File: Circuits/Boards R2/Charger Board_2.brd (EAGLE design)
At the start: 63.5 x 50.8 mm, 80 parts, among them CON1 ISP(2X3), CON10 HEADER_3X1, CON11 HEADER_3X1, CON12 HEADER_3X1, CON13 HEADER_4X1, CON2 SCREWTERMINAL_1X2, CON3 HEADER_3X1, CON4 HEADER_3X1, CON5 HEADER_3X1, CON6 HEADER_3X1, CON7 HEADER_3X1, CON8 HEADER_3X1, CON9 HEADER_3X1, IC1 NCP1117DT33G, T1 NPN2N2222, T2 NPN2N2222, T3 SI4421DY, U1 ATMEGA324P, U2 ACS711, U3 JOYSTICKPTH, U4 MX25L25735E

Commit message: 
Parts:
- added CON14, CON15: HEADER_3X1, Mechanical:3PINHEADER_.100"
- B1: value PIEZOBUZZER -> PIEZOBUZZERPTH; device Passive:PIEZOBUZZER_HORIZONTAL -> Passive:PIEZOBUZZER
- moved B1 205.6 mm to (-176.5, -27.9)
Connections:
- net +3V3: now also B1.1; no longer B1.P$1
- net N$9: now also B1.2; no longer B1.P$2
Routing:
- net +3V3: track 104.7 -> 99.7 mm
- net N$9: track 11.4 -> 8.90 mm
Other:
- board size 63.5 x 50.8 mm -> 101.6 x 81.3 mm
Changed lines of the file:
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@@
 <board>
 <plain>
-<wire x1="0" y1="0" x2="63.5" y2="0" width="0" layer="20"/>
-<wire x1="63.5" y1="0" x2="63.5" y2="50.8" width="0" layer="20"/>
-<wire x1="63.5" y1="50.8" x2="0" y2="50.8" width="0" layer="20"/>
-<wire x1="0" y1="50.8" x2="0" y2="0" width="0" layer="20"/>
+<wire x1="0" y1="0" x2="101.6" y2="0" width="0" layer="20"/>
+<wire x1="101.6" y1="0" x2="101.6" y2="81.28" width="0" layer="20"/>
+<wire x1="101.6" y1="81.28" x2="0" y2="81.28" width="0" layer="20"/>
+<wire x1="0" y1="81.28" x2="0" y2="0" width="0" layer="20"/>
 </plain>
 <attributes>
@@
 <element name="R7" library="Passive" package="0603" value="10k" x="6.35" y="27.94" rot="R270"/>
 <element name="CON1" library="Mechanical" package="PINHEADER(2X3)" value="ISP(2X3)" x="11.43" y="29.21" rot="R270"/>
-<element name="B1" library="Passive" package="PIEZOBUZZER_HORIZONTAL" value="PIEZOBUZZER" x="16.256" y="43.434"/>
 <element name="R8" library="Passive" package="0603" value="1k" x="6.35" y="41.91" rot="R90"/>
 <element name="T1" library="Passive" package="SOT23" value="NPN2N2222" x="8.89" y="38.1" rot="R180"/>
@@
 <element name="R23" library="Passive" package="0603" value="10k" x="-146.05" y="-34.29"/>
 <element name="R24" library="Passive" package="0603" value="10k" x="-149.86" y="-34.29"/>
+<element name="CON14" library="Mechanical" package="3PINHEADER_.100&quot;" value="HEADER_3X1" x="-156.21" y="-31.75"/>
+<element name="CON15" library="Mechanical" package="3PINHEADER_.100&quot;" value="HEADER_3X1" x="-165.1" y="-31.75"/>
+<element name="B1" library="Passive" package="PIEZOBUZZER" value="PIEZOBUZZERPTH" x="-176.53" y="-27.94"/>
 </elements>
 <signals>
@@
 </signal>
 <signal name="N$9">
-<contactref element="B1" pad="P$2"/>
 <contactref element="R8" pad="1"/>
 <contactref element="T1" pad="3"/>
@@
 <wire x1="8.66" y1="39.1" x2="6.35" y2="41.16" width="0.254" layer="1"/>
 <wire x1="8.89" y1="39.1" x2="14.462" y2="39.1" width="0.254" layer="1"/>
-<wire x1="14.462" y1="39.1" x2="16.256" y2="40.894" width="0.254" layer="1"/>
+<contactref element="B1" pad="2"/>
+<wire x1="6.35" y1="41.16" x2="-173.99" y2="-27.94" width="0" layer="19" extent="1-1"/>
 </signal>
 <signal name="N$10">
@@
 <contactref element="C1" pad="1"/>
 <contactref element="R8" pad="2"/>
-<contactref element="B1" pad="P$1"/>
 <contactref element="R7" pad="1"/>
 <contactref element="IC1" pad="2"/>
@@
 <wire x1="6.35" y1="29.972" x2="6.35" y2="29.21" width="0.254" layer="16"/>
 <wire x1="6.35" y1="42.66" x2="12.692" y2="42.41" width="0.254" layer="1"/>
-<wire x1="12.692" y1="42.41" x2="16.256" y2="45.974" width="0.254" layer="1"/>
 <wire x1="6.35" y1="42.66" x2="5.58" y2="42.41" width="0.254" layer="1"/>
 <wire x1="5.58" y1="42.41" x2="5.08" y2="41.91" width="0.254" layer="1"/>
@@
 <contactref element="C15" pad="1"/>
 <contactref element="R23" pad="1"/>
+<contactref element="B1" pad="1"/>
+<wire x1="-146.8" y1="-34.29" x2="-179.07" y2="-27.94" width="0" layer="19" extent="1-1"/>
 <wire x1="-142.99" y1="-34.29" x2="-146.8" y2="-34.29" width="0" layer="19" extent="1-1"/>
 <wire x1="-135.255" y1="-35.255" x2="-142.99" y2="-34.29" width="0" layer="19" extent="1-1"/>

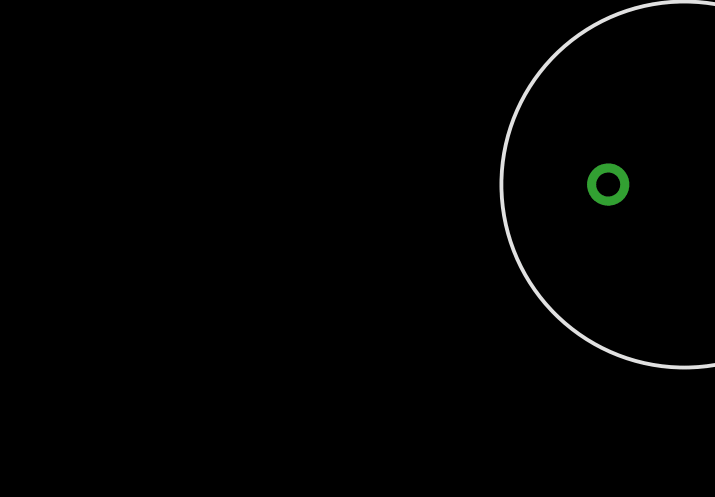
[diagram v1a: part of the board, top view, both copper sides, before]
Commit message: started adding rgb edge lighting hardware
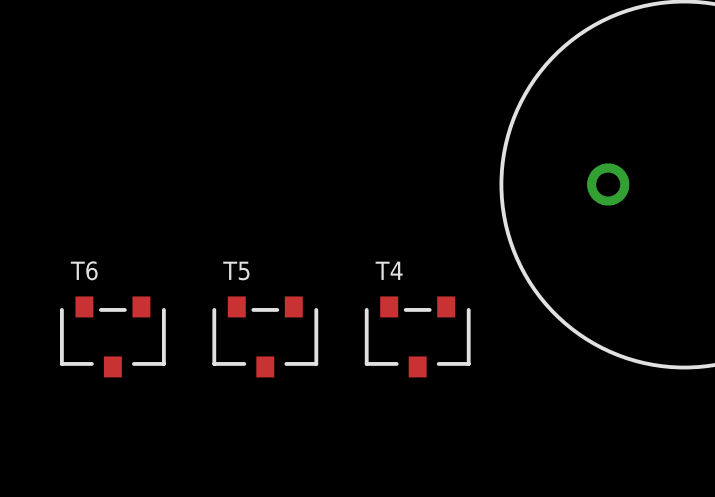
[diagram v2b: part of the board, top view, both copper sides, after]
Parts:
- added T4, T5, T6: NPN2N2222, Passive:SOT23
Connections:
- net GND: now also T4.2, T5.2, T6.2
- net LED1: now also T4.1
- net LED2: now also T5.1
- net LED3: now also T6.1
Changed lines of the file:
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@@
 <element name="CON15" library="Mechanical" package="3PINHEADER_.100&quot;" value="HEADER_3X1" x="-165.1" y="-31.75"/>
 <element name="B1" library="Passive" package="PIEZOBUZZER" value="PIEZOBUZZERPTH" x="-176.53" y="-27.94"/>
+<element name="T4" library="Passive" package="SOT23" value="NPN2N2222" x="-185.42" y="-33.02"/>
+<element name="T5" library="Passive" package="SOT23" value="NPN2N2222" x="-190.5" y="-33.02"/>
+<element name="T6" library="Passive" package="SOT23" value="NPN2N2222" x="-195.58" y="-33.02"/>
 </elements>
 <signals>
@@
 <contactref element="U4" pad="10"/>
 <contactref element="C15" pad="2"/>
+<contactref element="T4" pad="2"/>
+<contactref element="T5" pad="2"/>
+<contactref element="T6" pad="2"/>
+<wire x1="-191.45" y1="-32.02" x2="-196.53" y2="-32.02" width="0" layer="19" extent="1-1"/>
+<wire x1="-186.37" y1="-32.02" x2="-191.45" y2="-32.02" width="0" layer="19" extent="1-1"/>
+<wire x1="-141.49" y1="-34.29" x2="-186.37" y2="-32.02" width="0" layer="19" extent="1-1"/>
 <wire x1="-137.68" y1="-21.59" x2="-141.49" y2="-34.29" width="0" layer="19" extent="1-1"/>
 <wire x1="-134.0612" y1="-15.5194" x2="-137.68" y2="-21.59" width="0" layer="19" extent="1-1"/>
@@
 <wire x1="-18.05" y1="68.58" x2="-70.8" y2="61.96" width="0" layer="19" extent="1-1"/>
 <wire x1="9.84" y1="37.1" x2="-18.05" y2="68.58" width="0" layer="19" extent="1-1"/>
+<wire x1="12.7" y1="26.67" x2="11.43" y2="36.83" width="0" layer="19" extent="1-1"/>
+<wire x1="23.876" y1="29.21" x2="20.066" y2="25.4" width="0" layer="19" extent="1-1"/>
+<wire x1="28.321" y1="25.4" x2="24.13" y2="29.464" width="0" layer="19" extent="1-1"/>
+<wire x1="25.4" y1="21.59" x2="28.067" y2="25.146" width="0" layer="19" extent="1-1"/>
+<wire x1="39.37" y1="20.32" x2="32.25" y2="25.4" width="0" layer="19" extent="1-1"/>
+<wire x1="46.72" y1="25.4" x2="44.825" y2="20.955" width="0" layer="19" extent="1-1"/>
+<wire x1="3.81" y1="22.11" x2="12.7" y2="26.67" width="0" layer="19" extent="1-1"/>
+<wire x1="3.81" y1="15.24" x2="3.31" y2="20.82" width="0" layer="19" extent="1-1"/>
+<wire x1="3.81" y1="10.16" x2="3.81" y2="15.24" width="0" layer="19" extent="1-1"/>
+<wire x1="51.054" y1="12.954" x2="44.825" y2="20.955" width="0" layer="19" extent="1-1"/>
+<wire x1="13.97" y1="5.08" x2="3.81" y2="10.16" width="0" layer="19" extent="1-1"/>
+<wire x1="16.51" y1="5.08" x2="13.97" y2="5.08" width="0" layer="19" extent="1-1"/>
+<wire x1="19.05" y1="5.08" x2="16.51" y2="5.08" width="0" layer="19" extent="1-1"/>
+<wire x1="21.59" y1="5.08" x2="19.05" y2="5.08" width="0" layer="19" extent="1-1"/>
+<wire x1="24.13" y1="5.08" x2="21.59" y2="5.08" width="0" layer="19" extent="1-1"/>
+<wire x1="26.67" y1="5.08" x2="24.13" y2="5.08" width="0" layer="19" extent="1-1"/>
+<wire x1="29.21" y1="5.08" x2="26.67" y2="5.08" width="0" layer="19" extent="1-1"/>
+<wire x1="31.75" y1="5.08" x2="29.21" y2="5.08" width="0" layer="19" extent="1-1"/>
+<wire x1="34.29" y1="5.08" x2="31.75" y2="5.08" width="0" layer="19" extent="1-1"/>
+<wire x1="36.83" y1="5.08" x2="34.29" y2="5.08" width="0" layer="19" extent="1-1"/>
+<wire x1="58.42" y1="40.6" x2="53.705" y2="29.48" width="0" layer="19" extent="1-1"/>
 </signal>
 <signal name="RESET">
@@
 <wire x1="22.53" y1="31.15" x2="22.53" y2="33.85" width="0.254" layer="1"/>
 <contactref element="R21" pad="1"/>
+<contactref element="T4" pad="1"/>
+<wire x1="-66.79" y1="-8.89" x2="-184.47" y2="-32.02" width="0" layer="19" extent="1-1"/>
 <wire x1="22.53" y1="31.15" x2="-66.79" y2="-8.89" width="0" layer="19" extent="1-1"/>
 </signal>
@@
 <wire x1="21.73" y1="31.15" x2="21.73" y2="32.745" width="0.254" layer="1"/>
 <contactref element="R22" pad="1"/>
+<contactref element="T5" pad="1"/>
+<wire x1="-70.6" y1="-12.7" x2="-189.55" y2="-32.02" width="0" layer="19" extent="1-1"/>
 <wire x1="21.73" y1="31.15" x2="-70.6" y2="-12.7" width="0" layer="19" extent="1-1"/>
 </signal>
@@
 <contactref element="R1" pad="1"/>
 <contactref element="U1" pad="43"/>
+<contactref element="T6" pad="1"/>
+<wire x1="-70.6" y1="-8.89" x2="-194.63" y2="-32.02" width="0" layer="19" extent="1-1"/>
 <wire x1="20.93" y1="31.15" x2="-70.6" y2="-8.89" width="0" layer="19" extent="1-1"/>
 </signal>

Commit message: 
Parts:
- added C16, C19: 10uf, Passive:0805
- added C17, C18, C20, C21: .1uf, Passive:0603
- added CON16: HEADER_4X1, Mechanical:4PINHEADER_.100"
- added H5, H6, H7: MOUNTINGHOLE, Mechanical:MOUNTINGHOLE
- added LED7: IR, Passive:5MM_LED_RA
- added R25: 18, Passive:0603
- added R26, R29, R30: 1k, Passive:0603
- added T7, T8, T9: NPN2N2222, Passive:SOT23
- CON17, CON18: value FTDI_3PIN -> HEADER_3X1
- moved CON15 252.0 mm to (80.3, 25.4), turned to 90 degrees
- moved T6 248.5 mm to (46.0, 25.3), turned to 90 degrees
- moved T5 244.6 mm to (46.0, 29.5), turned to 90 degrees
- moved T4 240.8 mm to (46.0, 33.7), turned to 90 degrees
- moved CON14 231.6 mm to (63.0, 43.0), turned to 180 degrees
- moved B1 212.9 mm to (18.0, 58.5), turned to 270 degrees
- moved R24 212.9 mm to (59.4, 4.70)
- moved C12 207.1 mm to (85.7, 27.0), turned to 90 degrees
- moved C9 201.5 mm to (83.8, 27.0), turned to 90 degrees
- moved C8 200.1 mm to (84.8, 33.7), turned to 180 degrees
- moved C13 186.5 mm to (52.9, 39.9), turned to 270 degrees
- moved R15 184.8 mm to (54.9, 39.9), turned to 90 degrees
- moved R23 179.0 mm to (16.6, 40.3), turned to 90 degrees
- moved C15 174.8 mm to (17.3, 37.1)
- moved C7 171.7 mm to (89.5, 27.0), turned to 90 degrees
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- renumbered U$1 to CON17, U$2 to CON18
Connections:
- new net BLUE: CON16.1, T7.3
- new net GREEN: CON16.2, T8.3
- new net N$18: R26.1, T4.3, T7.1
- new net N$2: CON15.1, R16.1
- new net N$20: R29.1, T5.3, T8.1
- new net N$21: R30.1, T6.3, T9.1
- new net N$3: C12.1, C2.1, C6.1, C7.1, C8.1, C9.1, CON15.2, LED2.1, LED3.1, LED4.1, LED5.1, LED6.1, LED7.1
- new net N$5: C12.2, C2.2, C6.2, C7.2, C8.2, C9.2, CON15.3, T2.2
- new net N$6: LED7.2, R25.2
- new net RED: CON16.3, T9.3
- net +3V3: now also C16.1, C17.1, C18.1, C19.1, C20.1, C21.1, CON14.2
- net +5V: now also CON16.4, R26.2, R29.2, R30.2; no longer C12.1, C2.1, C6.1, C7.1, C8.1, C9.1, LED2.1, LED3.1, LED4.1, LED5.1, LED6.1
- net GND: now also C16.2, C17.2, C18.2, C19.2, C20.2, C21.2, CON14.3, CON17.1, CON18.1, T7.2, T8.2, T9.2; no longer C12.2, C2.2, C6.2, C7.2, C8.2, C9.2, CON17.3, CON18.3, T2.2
- net N$10: now also R25.1
- net N$19: now also CON18.3; no longer CON18.1
- net N$7: now also CON17.3; no longer CON17.1
- net TRANSMITLEDS: now also CON14.1; no longer R16.1
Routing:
- net +3V3: track 99.7 -> 229.9 mm, vias 4 -> 5
- net +5V: track 33.8 -> 121.2 mm
- net N$10: track 0.00 -> 68.4 mm
- net RESET: track 11.1 -> 54.3 mm
- net HORIZONTAL: track 0.00 -> 41.9 mm, vias 0 -> 2
- net TRANSMITLEDS: track 0.00 -> 41.3 mm
- net GND: track 39.6 -> 80.3 mm, vias 9 -> 15
- net VERTICAL: track 0.00 -> 37.9 mm
- net BUTTON: track 0.00 -> 36.4 mm
- net WP: track 0.00 -> 32.7 mm, vias 0 -> 2
- net LED3: track 0.00 -> 32.0 mm, vias 0 -> 2
- net LED2: track 1.59 -> 30.2 mm, vias 0 -> 2
- net CS: track 0.00 -> 26.7 mm, vias 0 -> 2
- net LED1: track 2.70 -> 28.8 mm, vias 0 -> 4
- net MISO: track 0.00 -> 25.0 mm
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- added copper zone on layer 1, net N$3
- added copper zone on layer 16, net N$5
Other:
- board size 101.6 x 81.3 mm -> 101.6 x 69.8 mm

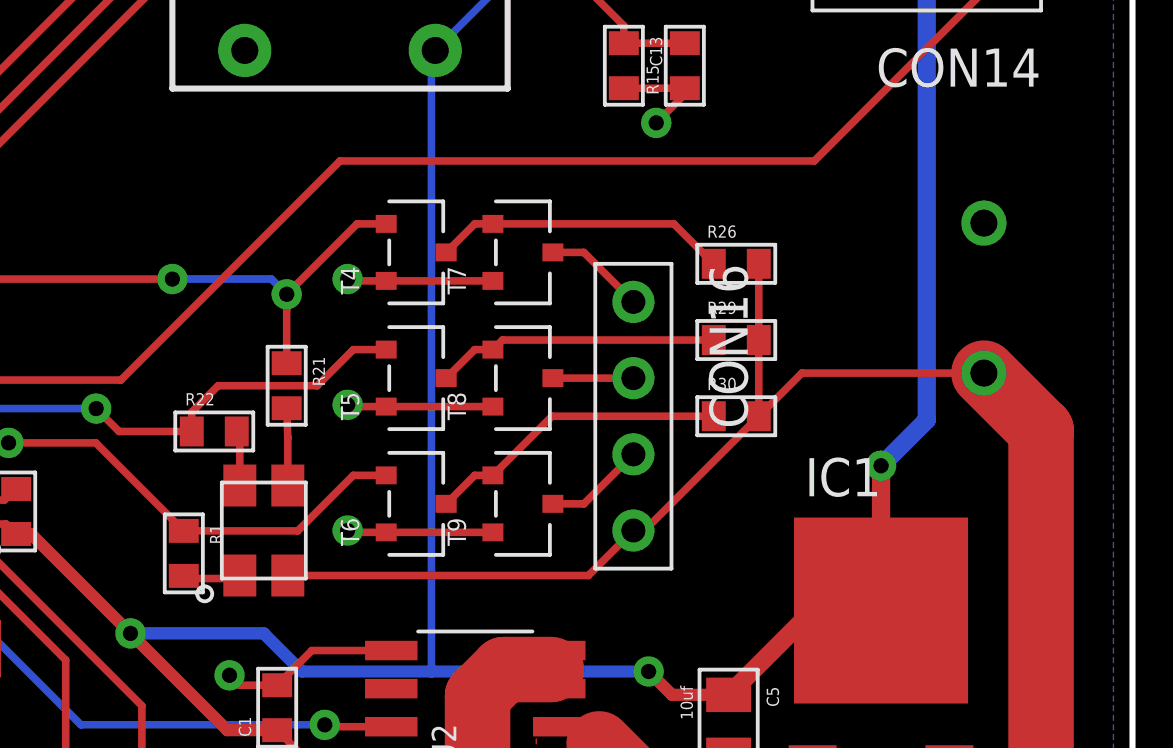
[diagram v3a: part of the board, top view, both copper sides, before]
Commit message: 
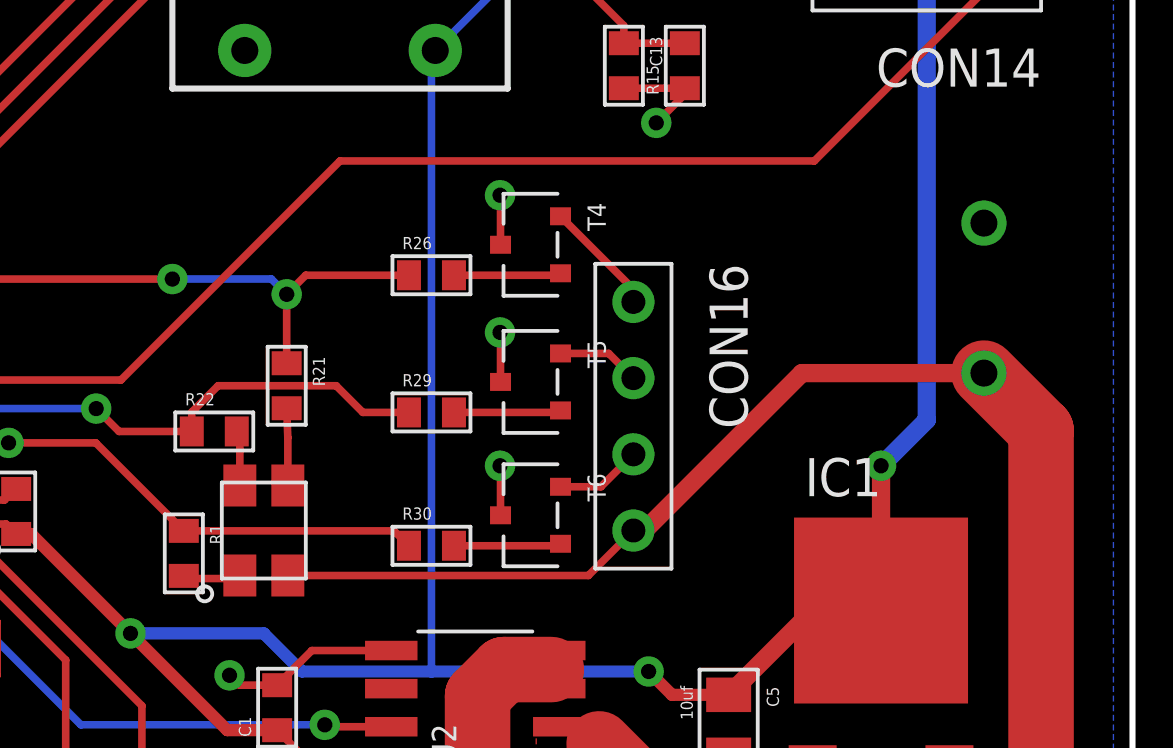
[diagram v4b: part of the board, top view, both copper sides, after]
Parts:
- removed T7, T8, T9: NPN2N2222, Passive:SOT23
- T4, T5, T6: value NPN2N2222 -> MMSS8550-L
- moved R30 11.0 mm to (46.5, 23.9)
- moved R29 10.4 mm to (46.5, 28.3)
- moved R26 10.2 mm to (46.5, 32.9)
- moved T6 3.83 mm to (49.8, 24.9), turned to 270 degrees
- moved T4 3.82 mm to (49.8, 33.9), turned to 270 degrees
- moved T5 3.81 mm to (49.8, 29.3), turned to 270 degrees
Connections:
- removed net N$18: R26.1, T4.3, T7.1
- removed net N$20: R29.1, T5.3, T8.1
- removed net N$21: R30.1, T6.3, T9.1
- new net N$36: R26.2, T4.1
- new net N$40: R29.2, T5.1
- new net N$41: R30.2, T6.1
- net +5V: no longer R26.2, R29.2, R30.2
- net BLUE: now also T4.2; no longer T7.3
- net GND: now also T4.3, T5.3, T6.3; no longer T4.2, T5.2, T6.2, T7.2, T8.2, T9.2
- net GREEN: now also T5.2; no longer T8.3
- net LED1: now also R26.1; no longer T4.1
- net LED2: now also R29.1; no longer T5.1
- net LED3: now also R30.1; no longer T6.1
- net RED: now also T6.2; no longer T9.3
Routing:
- net N$21: track 10.1 -> 0.00 mm
- net N$18: track 9.86 -> 0.00 mm
- net GND: track 80.3 -> 70.6 mm
- net N$20: track 9.44 -> 0.00 mm
- net +5V: track 121.2 -> 116.1 mm
- net N$36: track 0.00 -> 3.58 mm
- net N$41: track 0.00 -> 3.58 mm
- net N$40: track 0.00 -> 3.58 mm
- net LED2: track 30.2 -> 30.8 mm
